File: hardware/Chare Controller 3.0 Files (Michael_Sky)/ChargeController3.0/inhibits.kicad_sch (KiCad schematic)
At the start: 20 parts, among them J10 SOL_TEST_01x01_Pin, J11 GND_TEST_01x01_Pin, J19 SYS-1x2, J2 SP_01x02_Pin, J3 BATT_TEST_01x01_Pin, J5 BATT_01x02_Pin, J9 SYS_TEST_01x01_Pin, Q1 SI2318CDS-T1-GE3, Q10 SI2318CDS-T1-GE3, Q11 SI2318CDS-T1-GE3, Q13 SI2318CDS-T1-GE3, Q2 SI2318CDS-T1-GE3, Q3 SI2318CDS-T1-GE3, Q4 SI2318CDS-T1-GE3, Q9 SI2318CDS-T1-GE3, SW1 100SP1T1B1M1QEH

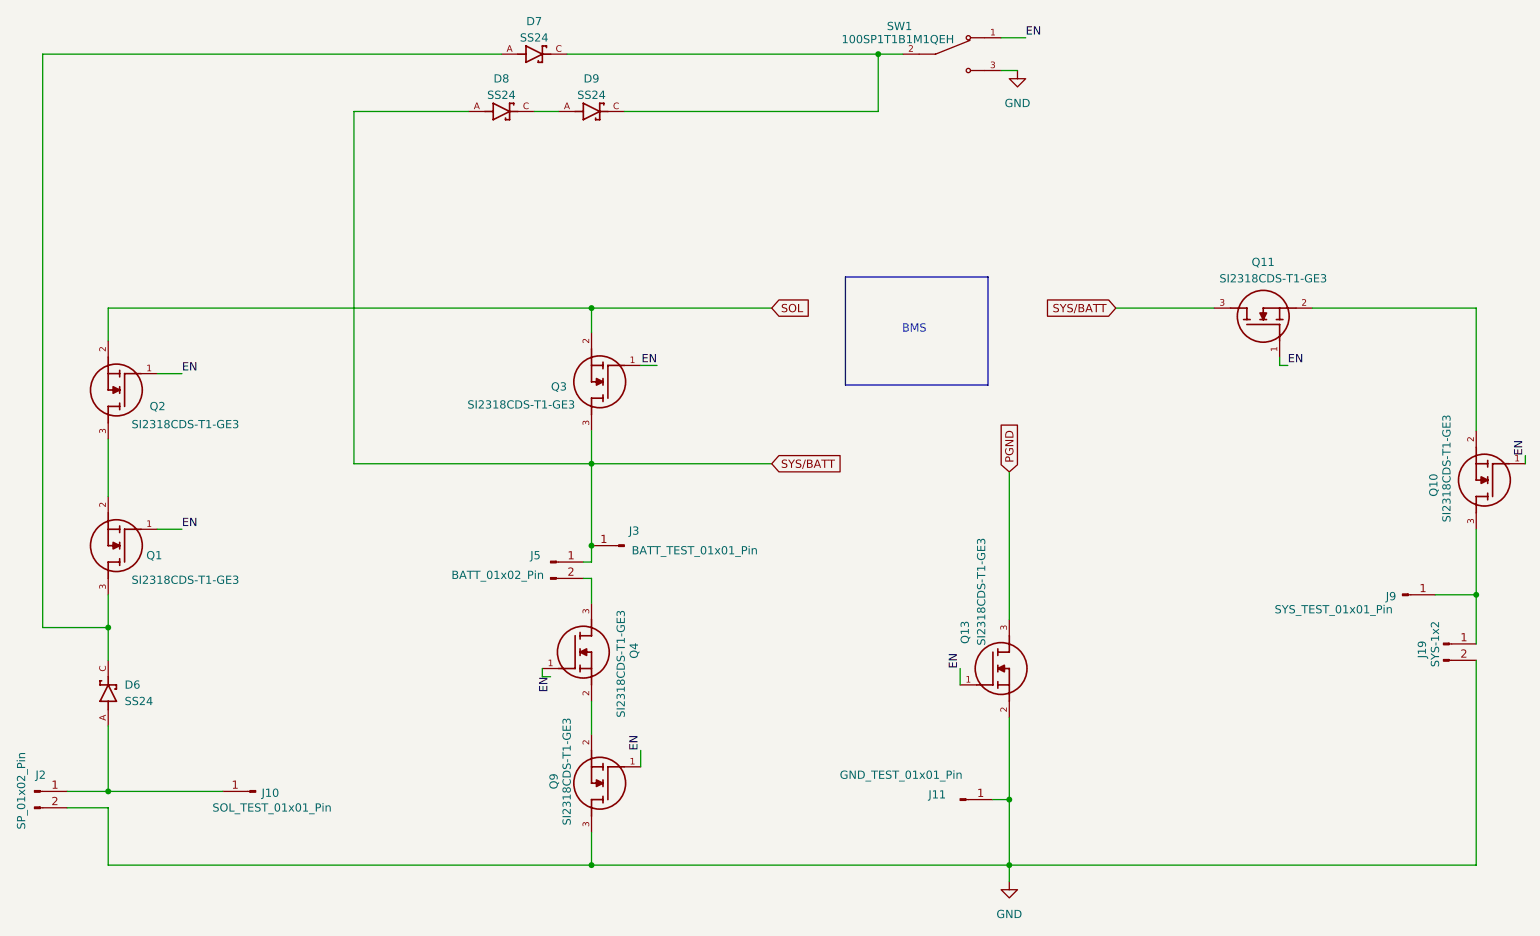
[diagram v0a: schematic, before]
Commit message: Grounding and Filtering, 3.0 Inhibits Updated
Grounding and Filtering, 3.0 Inhibits Updated
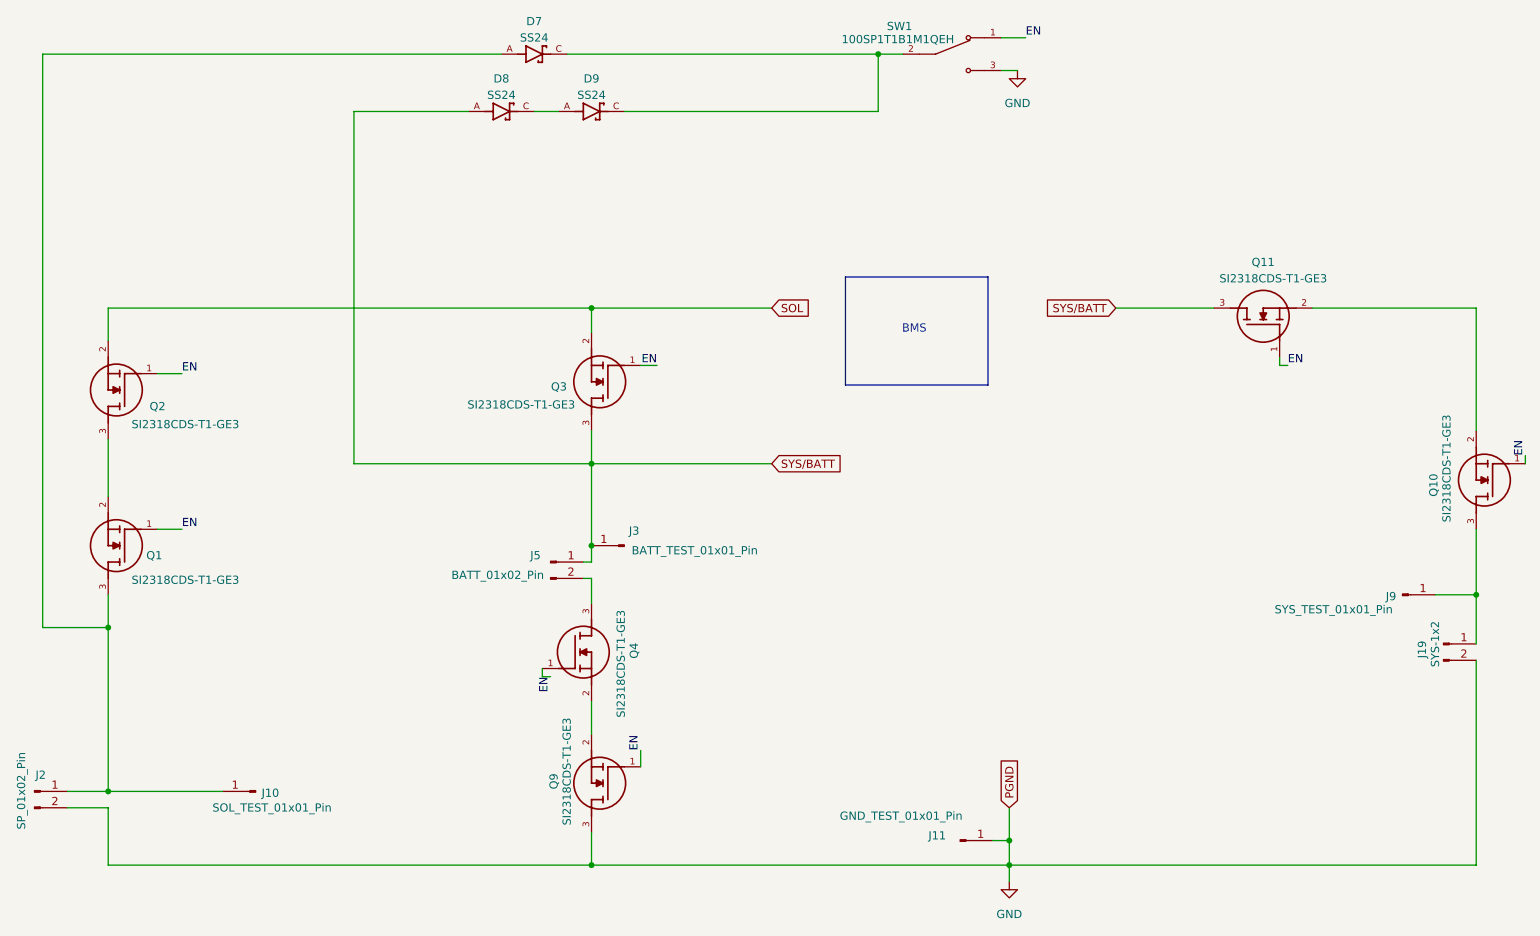
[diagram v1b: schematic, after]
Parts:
- removed D6: SS24, bmsfootprints:SS24, symbol SS24:SS24
- removed Q13: SI2318CDS-T1-GE3, bmsfootprints:SI2318CDS-T1-GE3, symbol SI2318CDS-T1-GE3:SI2318CDS-T1-GE3
- Q1, Q10, Q11, Q2, Q3, Q4, Q9: DESCRIPTION Vishay SI2318CDS-T1-GE3 N-channel MOSFET Transistor, 5.6 A,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 -> (none)
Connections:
- net at D7.A, Q1.3: now also J10.1 (Pin_1), J2.1 (Pin_1)
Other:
- moved on the sheet: J11
